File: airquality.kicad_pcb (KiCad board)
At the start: 2 copper layers, 99.9 x 99.9 mm, 26 parts, among them J1 MHZ19, J2 Conn_02x10_Odd_Even, J3 Conn_02x10_Odd_Even, J4 Conn_01x04_Female, J5 Conn_01x04_Male, J6 Conn_01x04_Female, J7 Conn_01x04_Male, J8 Conn_01x04_Male, U1 DS18B20, U2 PMS7003, U3 RFM95W-868S2, U4 DS18B20, U5 DS18B20

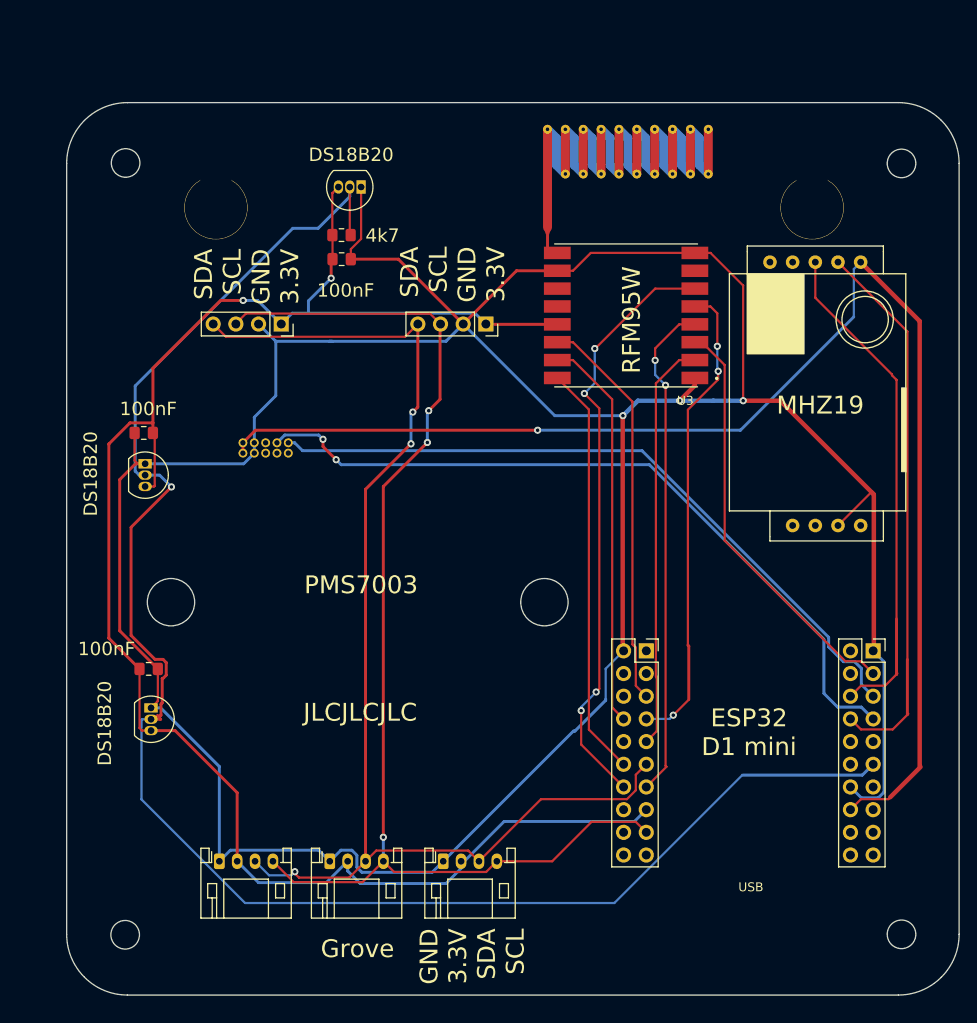
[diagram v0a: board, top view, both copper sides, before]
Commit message: minor silkscreen edit for jlcpcb
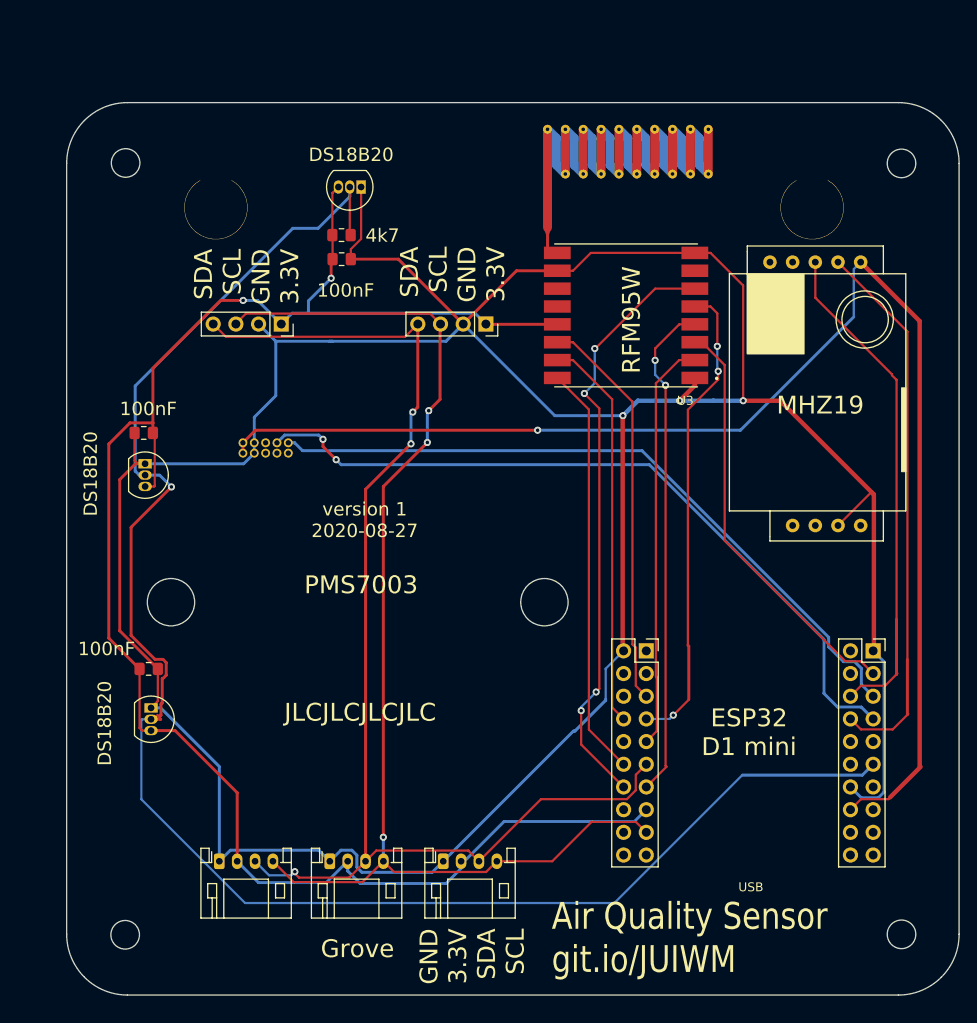
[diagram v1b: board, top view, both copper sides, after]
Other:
- board text added: "Air Quality Sensor git.io/JUIWM"
- board text added: "JLCJLCJLCJLC"
- board text added: "version 1 2020-08-27"
- board text removed: "JLCJLCJLC"

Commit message: rev2
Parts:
- removed AE1: Antenna, RF_Antenna:Texas_SWRA416_868MHz_915MHz
- removed C3: 100nF, Capacitor_SMD:C_0805_2012Metric_Pad1.15x1.40mm_HandSolder
- removed G*** (x2): LOGO, parts_models:keyhole
- removed REF** (x2): MountingHole_5.3mm_M5, MountingHole:MountingHole_5.3mm_M5
- removed REF** (x4): MountingHole_3.2mm_M3, MountingHole:MountingHole_3.2mm_M3
- removed the U3 at (163.6, 80.3)
- removed U5: DS18B20, Package_TO_SOT_THT:TO-92_Inline
- added C1: 100nF, Capacitor_SMD:C_0805_2012Metric_Pad1.15x1.40mm_HandSolder, F.Cu at (145.7, 103.2)
- added D1: SK6812, LED_SMD:LED_SK6812_PLCC4_5.0x5.0mm_P3.2mm, F.Cu at (145.7, 96.8)
- added H1: MountingHole, MountingHole:MountingHole_4.3mm_M4, F.Cu at (101.8, 109.2)
- added H2: MountingHole, MountingHole:MountingHole_4.3mm_M4, F.Cu at (141.2, 109.2)
- added H3: MountingHole, parts_models:keyhole, F.Cu at (175.3, 55.9)
- added H4: MountingHole, parts_models:keyhole, F.Cu at (104.5, 55.9)
- added H5: MountingHole, MountingHole:MountingHole_3.2mm_M3, F.Cu at (100.6, 52.0)
- added H6: MountingHole, MountingHole:MountingHole_3.2mm_M3, F.Cu at (190.6, 142.0)
- added H7: MountingHole, MountingHole:MountingHole_3.2mm_M3, F.Cu at (190.6, 52.0)
- added H8: MountingHole, MountingHole:MountingHole_3.2mm_M3, F.Cu at (100.6, 142.0)
- added J10: Conn_01x01_Male, Connector_PinHeader_2.54mm:PinHeader_1x01_P2.54mm_Vertical, F.Cu at (152.9, 120.8)
- added J11: Conn_01x01_Male, Connector_PinHeader_2.54mm:PinHeader_1x01_P2.54mm_Vertical, F.Cu at (152.9, 115.7)
- added J13: Conn_01x01_Male, Connector_PinHeader_2.54mm:PinHeader_1x01_P2.54mm_Vertical, F.Cu at (189.2, 123.3)
- added J14: Conn_01x01_Male, Connector_PinHeader_2.54mm:PinHeader_1x01_P2.54mm_Vertical, F.Cu at (189.1, 125.9)
- added J15: Conn_01x01_Male, Connector_PinHeader_2.54mm:PinHeader_1x01_P2.54mm_Vertical, F.Cu at (189.1, 128.5)
- added J16: Conn_01x01_Male, Connector_PinHeader_2.54mm:PinHeader_1x01_P2.54mm_Vertical, F.Cu at (189.2, 120.8)
- added J2: Conn_01x01_Male, Connector_PinHeader_2.54mm:PinHeader_1x01_P2.54mm_Vertical, F.Cu at (189.2, 105.5)
- added J22: Conn_01x01_Male, Connector_PinHeader_2.54mm:PinHeader_1x01_P2.54mm_Vertical, F.Cu at (189.2, 118.2)
- added J23: Conn_01x04_Female, Connector_PinSocket_2.54mm:PinSocket_1x04_P2.54mm_Vertical, F.Cu at (136.7, 64.2)
- added J24: Conn_01x04_Female, Connector_PinSocket_2.54mm:PinSocket_1x04_P2.54mm_Vertical, F.Cu at (118.0, 64.2)
- added J25: Conn_01x01_Male, Connector_PinHeader_2.54mm:PinHeader_1x01_P2.54mm_Vertical, F.Cu at (145.7, 109.1)
- added J3: Conn_01x01_Male, Connector_PinHeader_2.54mm:PinHeader_1x01_P2.54mm_Vertical, F.Cu at (189.2, 113.2)
- added J4: Conn_01x01_Male, Connector_PinHeader_2.54mm:PinHeader_1x01_P2.54mm_Vertical, F.Cu at (189.2, 115.7)
- added J5: Conn_01x01_Male, Connector_PinHeader_2.54mm:PinHeader_1x01_P2.54mm_Vertical, F.Cu at (152.9, 118.2)
- added J6: Conn_01x01_Male, Connector_PinHeader_2.54mm:PinHeader_1x01_P2.54mm_Vertical, F.Cu at (152.9, 125.9)
- added J7: Conn_01x01_Male, Connector_PinHeader_2.54mm:PinHeader_1x01_P2.54mm_Vertical, F.Cu at (152.9, 110.6)
- added J9: Conn_01x01_Male, Connector_PinHeader_2.54mm:PinHeader_1x01_P2.54mm_Vertical, F.Cu at (152.9, 113.2)
- added Q1: BSS138, Package_TO_SOT_SMD:SOT-23, F.Cu at (145.7, 83.3)
- added R1: 4k7, Resistor_SMD:R_0805_2012Metric_Pad1.15x1.40mm_HandSolder, F.Cu at (145.7, 78.7)
- added R2: 4k7, Resistor_SMD:R_0805_2012Metric_Pad1.15x1.40mm_HandSolder, F.Cu at (145.7, 129.0)
- added R3: 4k7, Resistor_SMD:R_0805_2012Metric_Pad1.15x1.40mm_HandSolder, F.Cu at (145.7, 88.3)
- added SW1: SW_Push, Button_Switch_SMD:SW_SPST_TL3342, F.Cu at (145.7, 135.4)
- J8: value Conn_01x04_Male -> Conn_01x01_Male; footprint Connector_JST:JST_PH_S4B-PH-K_1x04_P2.00mm_Horizontal -> Connector_PinHeader_2.54mm:PinHeader_1x01_P2.54mm_Vertical
- moved C5 31.9 mm to (100.1, 70.4)
- moved R4 31.9 mm to (100.1, 67.7)
- moved U2 31.9 mm to (102.3, 62.3)
- moved C6 31.4 mm to (98.5, 122.9)
- moved U3 22.8 mm to (98.6, 116.8)
- moved J8 20.5 mm to (152.9, 123.3)
- moved J17 19.5 mm to (159.0, 81.5), turned to 180 degrees
- moved J18 17.4 mm to (136.7, 67.9), turned to 90 degrees
- moved U1 17.3 mm to (121.5, 100.7)
- moved J1 16.0 mm to (160.0, 103.0)
- moved J12 16.0 mm to (185.4, 103.0)
- moved J20 15.9 mm to (108.9, 128.4)
- moved J21 15.9 mm to (121.2, 128.4)
- moved J19 15.1 mm to (118.0, 67.9), turned to 90 degrees
- renumbered C1 to C5, C2 to C6, J2 to J1, J3 to J12, J1 to J17, J4 to J18, J6 to J19, J5 to J20, J7 to J21, R1 to R4, U2 to U1, U1 to U2, U4 to U3
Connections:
- J1 pad 16: NC -> Net-(J1-Pad16)
- J1 pad 4: NC -> Net-(J1-Pad4)
- J17 pad 1: Net-(J1-Pad1) -> 5V
- J17 pad 3: 5V -> Net-(J17-Pad3)
- J8 pad 1: GND -> IO14
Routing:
- net IO14: track 67.8 -> 6.98 mm, vias 4 -> 0
- net IO15: track 0.00 -> 49.0 mm
- net 3.3V: track 194.5 -> 243.3 mm, vias 2 -> 0
- net IO18: track 53.2 -> 8.11 mm, vias 3 -> 0
- net IO5: track 56.1 -> 12.9 mm, vias 2 -> 0
- net IO27: track 46.8 -> 3.78 mm
- net IO34: track 46.3 -> 6.97 mm
- net IO35: track 44.3 -> 5.61 mm
- net IO19: track 46.0 -> 9.20 mm
- net GND: track 370.6 -> 337.7 mm, vias 3 -> 2
- net 1wire: track 188.7 -> 157.0 mm, vias 1 -> 0
- net I2C_SDA: track 138.9 -> 157.0 mm, vias 3 -> 2
- net 5V: track 151.0 -> 162.7 mm, vias 1 -> 3
- net Net-(D1-Pad2): track 0.00 -> 11.6 mm
- net IO22: track 56.3 -> 45.6 mm, vias 0 -> 1
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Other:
- outline, holes or cut-outs redrawn
- board text added: "14"
- board text added: "16"
- board text added: "17"
- board text added: "18"
- board text added: "19"
- board text added: "1W"
- board text added: "27"
- board text added: "33"
- board text added: "34"
- board text added: "35"
- board text added: "3v3"
- board text added: "5"
- board text added: "5v"
- board text added: "BSS138"
- board text added: "Careful which pinout you choose!"
- board text added: "Designed by @basoort"
- board text added: "GND"
- board text added: "LEDdata OUT"
- board text added: "Portal?"
- board text added: "SCL SDA GND 3.3V"
- board text added: "SDA SCL 3.3V GND"
- board text added: "SK6812"
- board text added: "version 2 2020-09-21"
- board text added: "“Snuffelaar”"
- board text removed: "RFM95W"
- board text removed: "version 1 2020-08-27"
